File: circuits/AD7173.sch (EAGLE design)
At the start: 17 parts, among them IC1 AD7173, IC2 LM3485, IC3 LM3485

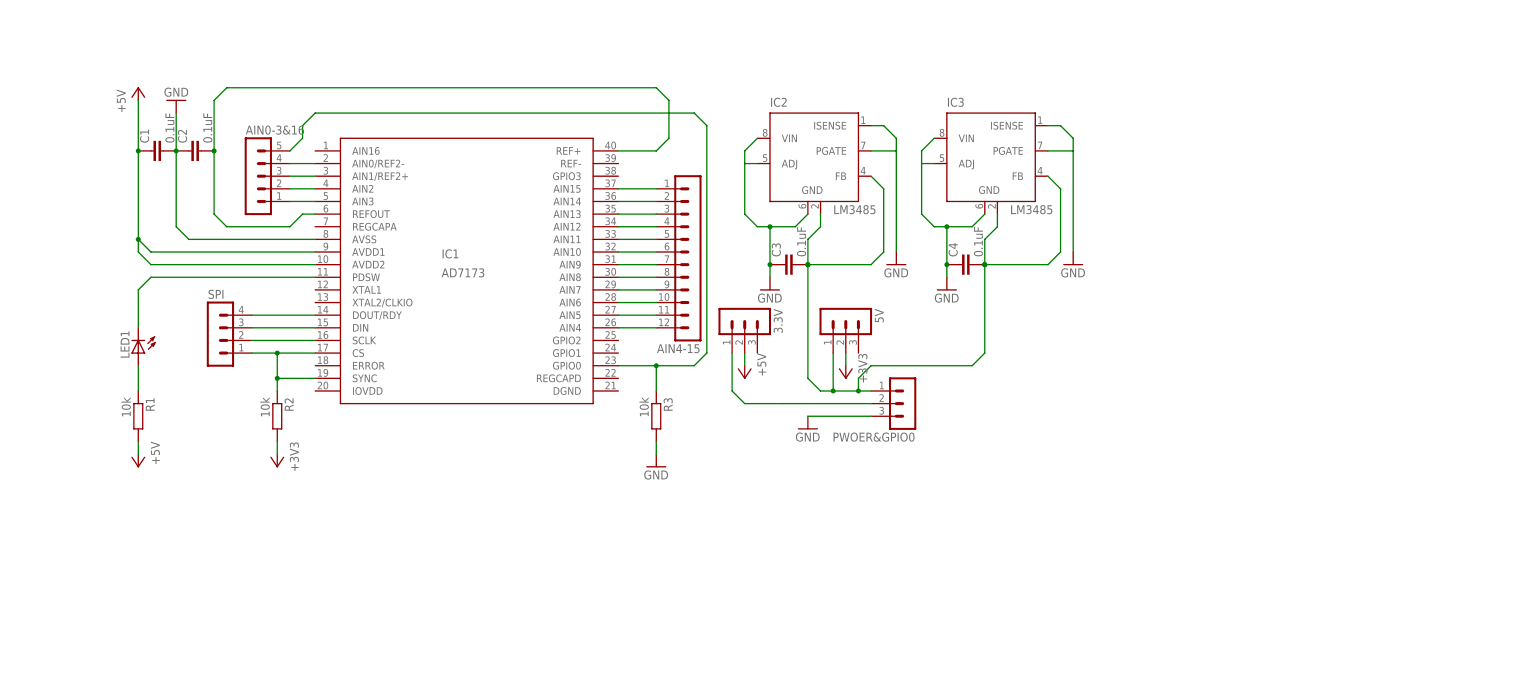
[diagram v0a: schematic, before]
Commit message: circuits/* updated eagle circuits
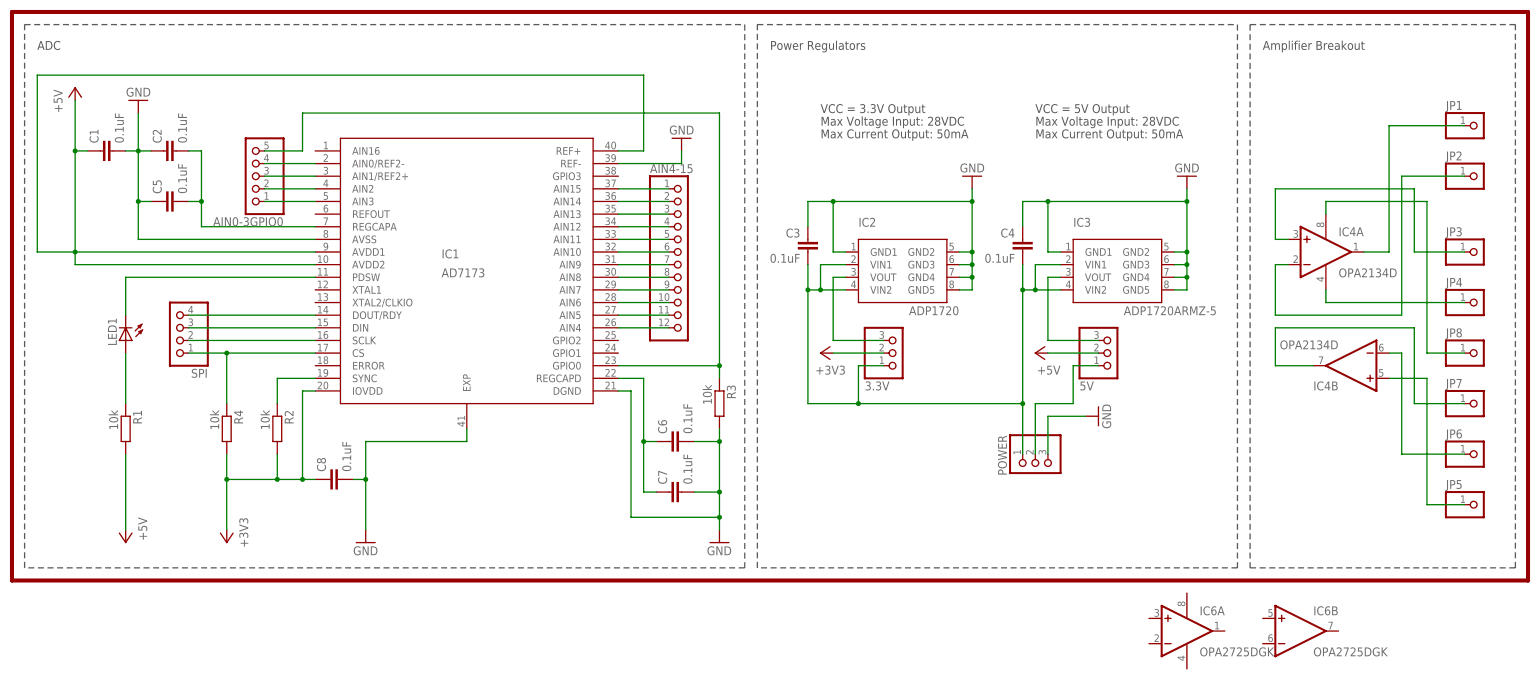
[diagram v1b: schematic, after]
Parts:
- removed AIN0-3&16: (no value), con-lstb:MA05-1
- removed PWOER&GPIO0: (no value), con-lstb:MA03-1
- added AIN0-3GPIO0: (no value), pinhead:PINHD-1X5
- added C5, C6, C7, C8: 0.1uF, rcl:C-EUC0402
- added IC4: OPA2134D, linear:OPA2134D
- added IC6: OPA2725DGK, linear:OPA2725DGK
- added JP1, JP2, JP3, JP4, JP5, JP6, JP7, JP8: (no value), pinhead:PINHD-1X1
- added POWER: (no value), pinhead:PINHD-1X3
- added R4: 10k, rcl:R-EU_R0402
- 3.3V, 5V: device con-lstb:MA03-1 -> pinhead:PINHD-1X3
- AIN4-15: device con-lstb:MA12-1 -> pinhead:PINHD-1X12
- IC2: value LM3485 -> ADP1720; device linear:LM3485 -> AD7173:POWER
- IC3: value LM3485 -> ADP1720ARMZ-5; device linear:LM3485 -> AD7173:POWER
- SPI: device con-lstb:MA04-1 -> pinhead:PINHD-1X4
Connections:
- new net N$28: 3.3V.1, C3.2, C4.2, IC2.VIN1, IC2.VIN2, IC3.VIN1, IC3.VIN2, POWER.1
- new net N$30: 5V.3, IC3.VOUT
- new net N$31: IC4A.OUT, JP1.1
- new net N$33: IC4A.-IN, JP2.1
- new net N$34: IC4A.+IN, JP3.1
- new net N$35: IC4P.V-, JP4.1
- new net N$36: IC4B.+IN, JP5.1
- new net N$37: IC4B.-IN, JP6.1
- new net N$38: C6.1, C7.1, IC1.REGCAPD
- new net N$39: IC1.SYNC, R2.1
- new net N$40: IC4B.OUT, JP7.1
- new net N$41: IC4P.V+, JP8.1
- net +3V3: now also 3.3V.2, C8.1, IC1.IOVDD, R4.2; no longer 5V.2
- net +5V: now also 5V.2, IC1.REF+; no longer 3.3V.2
- net GND: now also C5.1, C6.2, C7.2, C8.2, IC1.DGND, IC1.EXP, IC1.REF-, IC2.GND1, IC2.GND2, IC2.GND3, IC2.GND4, IC2.GND5, IC3.GND1, IC3.GND2, IC3.GND3, IC3.GND4, IC3.GND5, POWER.3; no longer IC2.ADJ, IC2.GND@1, IC2.ISENSE, IC2.PGATE, IC2.VIN, IC3.ADJ, IC3.GND@1, IC3.ISENSE, IC3.PGATE, IC3.VIN, PWOER&GPIO0.3
- net N$18: now also AIN0-3GPIO0.1; no longer AIN0-3&16.1
- net N$19: now also AIN0-3GPIO0.2; no longer AIN0-3&16.2
- net N$20: now also AIN0-3GPIO0.3; no longer AIN0-3&16.3
- net N$21: now also AIN0-3GPIO0.4; no longer AIN0-3&16.4
- net N$22: now also 5V.1, POWER.2; no longer 3.3V.1, PWOER&GPIO0.2
- net N$27: now also 3.3V.3, IC2.VOUT; no longer 5V.1, C3.2, C4.2, IC2.FB, IC2.GND@2, IC3.FB, IC3.GND@2, PWOER&GPIO0.1
- net N$3: now also R4.1; no longer IC1.SYNC, R2.1
- net N$5: now also AIN0-3GPIO0.5; no longer AIN0-3&16.5
- net N$6: now also C5.2, IC1.REGCAPA; no longer IC1.REF+, IC1.REFOUT
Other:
- note added: "ADC"
- note added: "Amplifier Breakout"
- note added: "Max Current Output: 50mA"
- note added: "Max Voltage Input: 28VDC"
- note added: "Power Regulators"
- note added: "VCC = 3.3V Output"
- note added: "VCC = 5V Output"
- moved on the sheet: C1, C2, C3, C4, LED1, R1, R2, R3
